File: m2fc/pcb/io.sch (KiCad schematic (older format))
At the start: 35 parts, among them IC401 ADuM5201, IC402 ADuM1201, P401 CONN_4, P402 CONN_2, P403 CONN_4, U401 HOUSING, U402 RG LED, U403 HOUSING, U404 HOUSING

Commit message: m2fc footprints, start layout
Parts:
- removed C401, C402: 10µ, m2fc:C0603, symbol CP1
- added C401, C402: 10µ, m2fc:C0603, symbol C
- IC401: footprint (none) -> m2fc:SOIC16
- IC402: Farnell (none) -> 1078200
- P401, P403: Farnell (none) -> 1830749
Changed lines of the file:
@@
 F 2 "m2fc:S04B-PASK-2" H 6150 3350 60  0001 C CNN
 F 3 "" H 6150 3350 60  0001 C CNN
-F 4 "512-8484" V 6150 3350 60  0001 C CNN "RS"
+F 4 "1830749" H 6150 3350 60  0001 C CNN "Farnell"
+F 5 "512-8484" V 6150 3350 60  0001 C CNN "RS"
 	1    6150 3350
 	1    0    0    -1
@@
 F 0 "IC401" H 4500 3800 60  0000 C CNN
 F 1 "ADuM5201" H 4650 2900 60  0000 C CNN
-F 2 "" H 4800 3400 60  0001 C CNN
+F 2 "m2fc:SOIC16" H 4800 3400 60  0001 C CNN
 F 3 "" H 4800 3400 60  0000 C CNN
 F 4 "2067773" H 4700 3400 60  0001 C CNN "Farnell"
@@
 $EndComp
 $Comp
-L CP1 C401
-U 1 1 53B6A643
-P 4000 2600
-F 0 "C401" H 4050 2700 50  0000 L CNN
-F 1 "10µ" H 4050 2500 50  0000 L CNN
-F 2 "m2fc:C0603" H 4000 2600 60  0001 C CNN
-F 3 "" H 4000 2600 60  0001 C CNN
-F 4 "1657936" H 4000 2600 60  0001 C CNN "Farnell"
-	1    4000 2600
-	0    1    -1   0
-$EndComp
-$Comp
 L C C404
 U 1 1 53B6A64B
@@
 $EndComp
 $Comp
-L CP1 C402
-U 1 1 53B6A653
-P 5450 2700
-F 0 "C402" H 5500 2800 50  0000 L CNN
-F 1 "10µ" H 5500 2600 50  0000 L CNN
-F 2 "m2fc:C0603" H 5450 2700 60  0001 C CNN
-F 3 "" H 5450 2700 60  0001 C CNN
-F 4 "1657936" H 5450 2700 60  0001 C CNN "Farnell"
-	1    5450 2700
-	0    -1   -1   0
-$EndComp
-$Comp
-L GND #PWR408
+L GND #PWR0129
 U 1 1 53B6A65A
 P 4200 3500
-F 0 "#PWR408" H 4200 3500 30  0001 C CNN
+F 0 "#PWR0129" H 4200 3500 30  0001 C CNN
 F 1 "GND" H 4200 3430 30  0001 C CNN
 F 2 "" H 4200 3500 60  0001 C CNN
@@
 $EndComp
 $Comp
-L GND #PWR411
+L GND #PWR0130
 U 1 1 53B6A660
 P 4250 3850
-F 0 "#PWR411" H 4250 3850 30  0001 C CNN
+F 0 "#PWR0130" H 4250 3850 30  0001 C CNN
 F 1 "GND" H 4250 3780 30  0001 C CNN
 F 2 "" H 4250 3850 60  0001 C CNN
@@
 $EndComp
 $Comp
-L GND #PWR406
+L GND #PWR0131
 U 1 1 53B6A668
 P 3750 3100
-F 0 "#PWR406" H 3750 3100 30  0001 C CNN
+F 0 "#PWR0131" H 3750 3100 30  0001 C CNN
 F 1 "GND" H 3750 3030 30  0001 C CNN
 F 2 "" H 3750 3100 60  0001 C CNN
@@
 SERIAL IN/OUT 1
 $Comp
-L +3.3V #PWR410
+L +3.3V #PWR0132
 U 1 1 53B6A6B9
 P 4100 3600
-F 0 "#PWR410" H 4100 3560 30  0001 C CNN
+F 0 "#PWR0132" H 4100 3560 30  0001 C CNN
 F 1 "+3.3V" H 4100 3710 30  0000 C CNN
 F 2 "" H 4100 3600 60  0000 C CNN
@@
 $EndComp
 $Comp
-L GND #PWR403
+L GND #PWR0133
 U 1 1 53B6B193
 P 7600 2550
-F 0 "#PWR403" H 7600 2550 30  0001 C CNN
+F 0 "#PWR0133" H 7600 2550 30  0001 C CNN
 F 1 "GND" H 7600 2480 30  0001 C CNN
 F 2 "" H 7600 2550 60  0001 C CNN
@@
 $EndComp
 $Comp
-L GND #PWR404
+L GND #PWR0134
 U 1 1 53B6B1AA
 P 7950 2800
-F 0 "#PWR404" H 7950 2800 30  0001 C CNN
+F 0 "#PWR0134" H 7950 2800 30  0001 C CNN
 F 1 "GND" H 7950 2730 30  0001 C CNN
 F 2 "" H 7950 2800 60  0001 C CNN
@@
 $EndComp
 $Comp
-L GND #PWR405
+L GND #PWR0135
 U 1 1 53B6B1C1
 P 7950 3050
-F 0 "#PWR405" H 7950 3050 30  0001 C CNN
+F 0 "#PWR0135" H 7950 3050 30  0001 C CNN
 F 1 "GND" H 7950 2980 30  0001 C CNN
 F 2 "" H 7950 3050 60  0001 C CNN
@@
 $EndComp
 $Comp
-L GND #PWR407
+L GND #PWR0136
 U 1 1 53B6B1D8
 P 7950 3300
-F 0 "#PWR407" H 7950 3300 30  0001 C CNN
+F 0 "#PWR0136" H 7950 3300 30  0001 C CNN
 F 1 "GND" H 7950 3230 30  0001 C CNN
 F 2 "" H 7950 3300 60  0001 C CNN
@@
 INTERNAL STATUS LEDS
 $Comp
-L +3.3V #PWR401
+L +3.3V #PWR0137
 U 1 1 53B6B1DF
 P 6550 2450
-F 0 "#PWR401" H 6550 2410 30  0001 C CNN
+F 0 "#PWR0137" H 6550 2410 30  0001 C CNN
 F 1 "+3.3V" H 6550 2560 30  0000 C CNN
 F 2 "" H 6550 2450 60  0000 C CNN
@@
 $EndComp
 $Comp
-L GND #PWR417
+L GND #PWR0138
 U 1 1 53BB3222
 P 7150 4800
-F 0 "#PWR417" H 7150 4800 30  0001 C CNN
+F 0 "#PWR0138" H 7150 4800 30  0001 C CNN
 F 1 "GND" H 7150 4730 30  0001 C CNN
 F 2 "" H 7150 4800 60  0001 C CNN
@@
 $EndComp
 $Comp
-L GND #PWR412
+L GND #PWR0139
 U 1 1 53BB32F5
 P 7150 4100
-F 0 "#PWR412" H 7150 4100 30  0001 C CNN
+F 0 "#PWR0139" H 7150 4100 30  0001 C CNN
 F 1 "GND" H 7150 4030 30  0001 C CNN
 F 2 "" H 7150 4100 60  0001 C CNN
@@
 INPUT/OUTPUT
 $Comp
-L +3.3V #PWR402
+L +3.3V #PWR0140
 U 1 1 53C7FC56
 P 4250 2550
-F 0 "#PWR402" H 4250 2510 30  0001 C CNN
+F 0 "#PWR0140" H 4250 2510 30  0001 C CNN
 F 1 "+3.3V" H 4250 2660 30  0000 C CNN
 F 2 "" H 4250 2550 60  0000 C CNN
@@
 F 2 "m2fc:S04B-PASK-2" H 6150 4550 60  0001 C CNN
 F 3 "" H 6150 4550 60  0001 C CNN
-F 4 "512-8484" V 6150 4550 60  0001 C CNN "RS"
+F 4 "1830749" H 6150 4550 60  0001 C CNN "Farnell"
+F 5 "512-8484" V 6150 4550 60  0001 C CNN "RS"
 	1    6150 4550
 	1    0    0    -1
@@
 $EndComp
 $Comp
-L +3.3V #PWR414
+L +3.3V #PWR0141
 U 1 1 53C90EC1
 P 4300 4350
-F 0 "#PWR414" H 4300 4310 30  0001 C CNN
+F 0 "#PWR0141" H 4300 4310 30  0001 C CNN
 F 1 "+3.3V" H 4300 4460 30  0000 C CNN
 F 2 "" H 4300 4350 60  0000 C CNN
@@
 F 2 "m2fc:SOIC8" H 4700 4550 60  0001 C CNN
 F 3 "" H 4700 4550 60  0000 C CNN
+F 4 "1078200" H 4700 4550 60  0001 C CNN "Farnell"
 	1    4700 4550
 	1    0    0    -1
 $EndComp
 $Comp
-L GND #PWR415
+L GND #PWR0142
 U 1 1 53C90E72
 P 4300 4750
-F 0 "#PWR415" H 4300 4750 30  0001 C CNN
+F 0 "#PWR0142" H 4300 4750 30  0001 C CNN
 F 1 "GND" H 4300 4680 30  0001 C CNN
 F 2 "" H 4300 4750 60  0001 C CNN
@@
 	6350 5300 8150 5300
 $Comp
-L PWR_FLAG #FLG401
+L PWR_FLAG #FLG0143
 U 1 1 53D4CBCD
 P 5750 4350
-F 0 "#FLG401" H 5750 4445 30  0001 C CNN
+F 0 "#FLG0143" H 5750 4445 30  0001 C CNN
 F 1 "PWR_FLAG" H 5750 4530 30  0000 C CNN
 F 2 "" H 5750 4350 60  0000 C CNN
@@
 $EndComp
 $Comp
-L PWR_FLAG #FLG402
+L PWR_FLAG #FLG0144
 U 1 1 53D4CC1D
 P 5750 4750
-F 0 "#FLG402" H 5750 4845 30  0001 C CNN
+F 0 "#FLG0144" H 5750 4845 30  0001 C CNN
 F 1 "PWR_FLAG" H 5750 4930 30  0000 C CNN
 F 2 "" H 5750 4750 60  0000 C CNN
@@
 $EndComp
 $Comp
-L GND #PWR409
+L GND #PWR0145
 U 1 1 53D79DC5
 P 7950 3550
-F 0 "#PWR409" H 7950 3550 30  0001 C CNN
+F 0 "#PWR0145" H 7950 3550 30  0001 C CNN
 F 1 "GND" H 7950 3480 30  0001 C CNN
 F 2 "" H 7950 3550 60  0001 C CNN
@@
 Connection ~ 7600 4150
 $Comp
-L GND #PWR413
+L GND #PWR0146
 U 1 1 53DA7B01
 P 7900 4200
-F 0 "#PWR413" H 7900 4200 30  0001 C CNN
+F 0 "#PWR0146" H 7900 4200 30  0001 C CNN
 F 1 "GND" H 7900 4130 30  0001 C CNN
 F 2 "" H 7900 4200 60  0001 C CNN
@@
 	7900 4150 7900 4200
 $Comp
-L GND #PWR416
+L GND #PWR0147
 U 1 1 53DA7BD9
 P 7900 4750
-F 0 "#PWR416" H 7900 4750 30  0001 C CNN
+F 0 "#PWR0147" H 7900 4750 30  0001 C CNN
 F 1 "GND" H 7900 4680 30  0001 C CNN
 F 2 "" H 7900 4750 60  0001 C CNN
@@
 Wire Wire Line
 	7900 4700 7900 4750
+$Comp
+L C C402
+U 1 1 53D87AE9
+P 5450 2700
+F 0 "C402" H 5500 2800 50  0000 L CNN
+F 1 "10µ" H 5500 2600 50  0000 L CNN
+F 2 "m2fc:C0603" H 5450 2700 60  0001 C CNN
+F 3 "" H 5450 2700 60  0001 C CNN
+F 4 "2211164" H 5450 2700 60  0001 C CNN "Farnell"
+	1    5450 2700
+	0    -1   -1   0
+$EndComp
+$Comp
+L C C401
+U 1 1 53D87C19
+P 4000 2600
+F 0 "C401" H 4050 2700 50  0000 L CNN
+F 1 "10µ" H 4050 2500 50  0000 L CNN
+F 2 "m2fc:C0603" H 4000 2600 60  0001 C CNN
+F 3 "" H 4000 2600 60  0001 C CNN
+F 4 "2211164" H 4000 2600 60  0001 C CNN "Farnell"
+	1    4000 2600
+	0    -1   -1   0
+$EndComp
 $EndSCHEMATC

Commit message: layout going ok so far...
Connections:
- net GND: now also D407.1; no longer D407.2
- net LED_C: now also D407.2; no longer D407.1
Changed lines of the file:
@@
 L CGA0402MLC-12G D407
 U 1 1 53DA782A
-P 7650 4700
-F 0 "D407" H 7750 4600 60  0000 C CNN
-F 1 "CGA0402MLC-12G" H 7750 4810 60  0001 C CNN
-F 2 "m2fc:R0402" H 7650 4700 60  0001 C CNN
-F 3 "" H 7650 4700 60  0000 C CNN
-F 4 "2368169" H 7650 4700 60  0001 C CNN "Farnell"
-	1    7650 4700
-	1    0    0    -1
+P 7850 4700
+F 0 "D407" H 7950 4600 60  0000 C CNN
+F 1 "CGA0402MLC-12G" H 7950 4810 60  0001 C CNN
+F 2 "m2fc:R0402" H 7850 4700 60  0001 C CNN
+F 3 "" H 7850 4700 60  0000 C CNN
+F 4 "2368169" H 7850 4700 60  0001 C CNN "Farnell"
+	1    7850 4700
+	-1   0    0    1
 $EndComp
 Wire Wire Line

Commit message: flip around power connectors
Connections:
- net SER_IN_2: now also IC402.2 (OUT_A), TP403.1 (TP); no longer IC402.3 (IN_B), TP404.1 (TP)
- net SER_OUT_2: now also IC402.3 (IN_B), TP404.1 (TP); no longer IC402.2 (OUT_A), TP403.1 (TP)
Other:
- note added: "NB Different Serial Pinouts"
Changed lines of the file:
@@
 Text Notes 3350 5250 0    60   ~ 0
 SERIAL IN/OUT 2
-Text HLabel 4000 4500 0    60   Input ~ 0
+Text HLabel 4000 4600 0    60   Input ~ 0
 SER_OUT_2
-Text HLabel 4000 4600 0    60   Output ~ 0
+Text HLabel 4000 4500 0    60   Output ~ 0
 SER_IN_2
 $Comp
@@
 	0    -1   -1   0
 $EndComp
+Text Notes 3350 5100 0    60   ~ 0
+NB Different Serial Pinouts
 $EndSCHEMATC

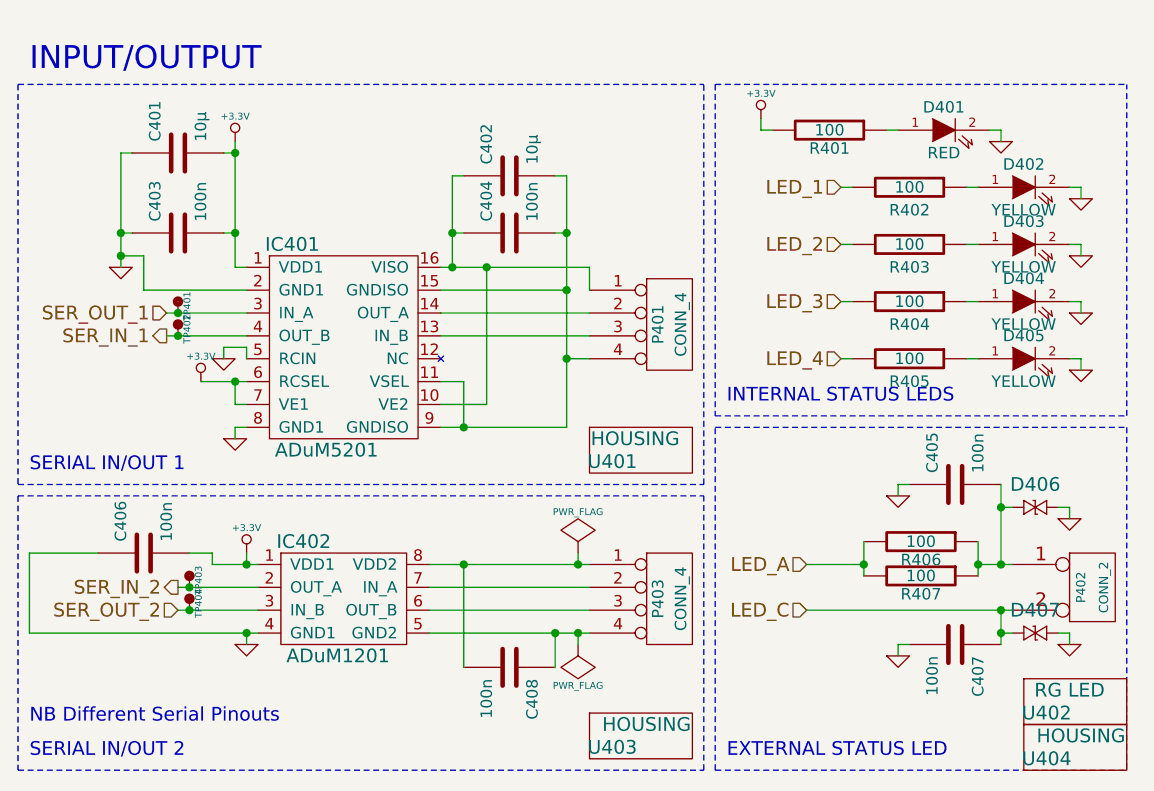
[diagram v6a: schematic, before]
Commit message: 3V ANALOG LED
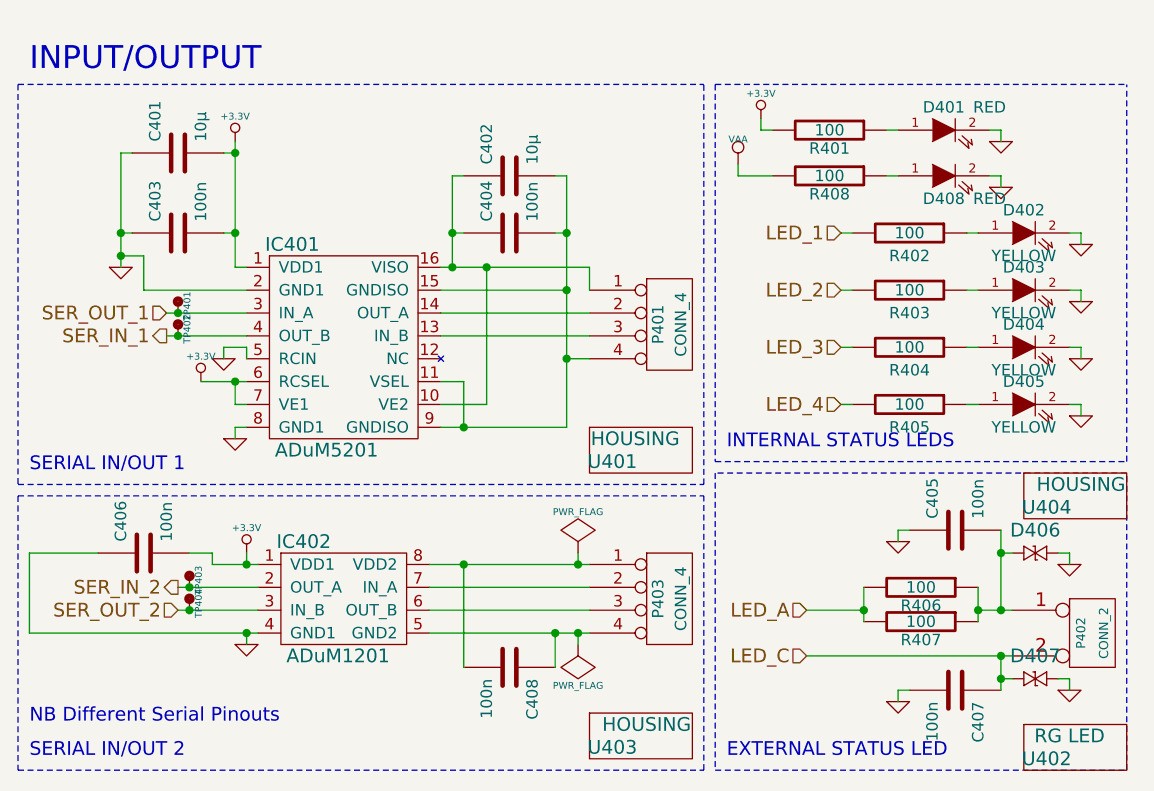
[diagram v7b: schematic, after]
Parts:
- added D408: RED, m2fc:LED0603, symbol LED
- added R408: 100, m2fc:R0603, symbol R
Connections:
- net GND: now also D408.2 (K)
- new net: D408.1 (A), R408.1
- new net VAA: R408.2
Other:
- moved on the sheet: C405, C407, D402, D403, D404, D405, D406, D407, P402, R402, R403, R404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

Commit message: rescue symbols from m2fc pcb
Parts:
- C401, C402, C403, C404, C405, C406, C407, C408: symbol C -> C-RESCUE-m2fc
- D401, D402, D403, D404, D405, D408: symbol LED -> LED-RESCUE-m2fc
- R401, R402, R403, R404, R405, R406, R407, R408: symbol R -> R-RESCUE-m2fc
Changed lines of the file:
@@
 EESchema Schematic File Version 2
+LIBS:m2fc-rescue
 LIBS:power
 LIBS:device
@@
 LIBS:memory
 LIBS:xilinx
-LIBS:special
 LIBS:microcontrollers
 LIBS:dsp
@@
 LIBS:cga0402mlc-12g
 LIBS:m2fc-cache
-EELAYER 24 0
+EELAYER 25 0
 EELAYER END
 $Descr A4 11693 8268
@@
 $EndComp
 $Comp
-L C C403
+L C-RESCUE-m2fc C403
 U 1 1 53B6A63B
 P 4000 2950
@@
 $EndComp
 $Comp
-L C C404
+L C-RESCUE-m2fc C404
 U 1 1 53B6A64B
 P 5450 2950
@@
 $EndComp
 $Comp
-L GND #PWR0134
+L GND-RESCUE-m2fc #PWR0134
 U 1 1 53B6A65A
 P 4200 3500
@@
 $EndComp
 $Comp
-L GND #PWR0135
+L GND-RESCUE-m2fc #PWR0135
 U 1 1 53B6A660
 P 4250 3850
@@
 $EndComp
 $Comp
-L GND #PWR0136
+L GND-RESCUE-m2fc #PWR0136
 U 1 1 53B6A668
 P 3750 3100
@@
 SERIAL IN/OUT 1
 $Comp
-L +3.3V #PWR0137
+L +3.3V-RESCUE-m2fc #PWR0137
 U 1 1 53B6A6B9
 P 4100 3600
@@
 $EndComp
 $Comp
-L R R407
+L R-RESCUE-m2fc R407
 U 1 1 53B6AD98
 P 7250 4650
@@
 $EndComp
 $Comp
-L R R406
+L R-RESCUE-m2fc R406
 U 1 1 53B6ADA0
 P 7250 4500
@@
 $EndComp
 $Comp
-L LED D401
+L LED-RESCUE-m2fc D401
 U 1 1 53B6B184
 P 7350 2500
@@
 $EndComp
 $Comp
-L R R401
+L R-RESCUE-m2fc R401
 U 1 1 53B6B18C
 P 6850 2500
@@
 $EndComp
 $Comp
-L GND #PWR0138
+L GND-RESCUE-m2fc #PWR0138
 U 1 1 53B6B193
 P 7600 2550
@@
 $EndComp
 $Comp
-L LED D402
+L LED-RESCUE-m2fc D402
 U 1 1 53B6B19B
 P 7700 2950
@@
 $EndComp
 $Comp
-L R R402
+L R-RESCUE-m2fc R402
 U 1 1 53B6B1A3
 P 7200 2950
@@
 $EndComp
 $Comp
-L GND #PWR0139
+L GND-RESCUE-m2fc #PWR0139
 U 1 1 53B6B1AA
 P 7950 3000
@@
 $EndComp
 $Comp
-L LED D403
+L LED-RESCUE-m2fc D403
 U 1 1 53B6B1B2
 P 7700 3200
@@
 $EndComp
 $Comp
-L R R403
+L R-RESCUE-m2fc R403
 U 1 1 53B6B1BA
 P 7200 3200
@@
 $EndComp
 $Comp
-L GND #PWR0140
+L GND-RESCUE-m2fc #PWR0140
 U 1 1 53B6B1C1
 P 7950 3250
@@
 $EndComp
 $Comp
-L LED D404
+L LED-RESCUE-m2fc D404
 U 1 1 53B6B1C9
 P 7700 3450
@@
 $EndComp
 $Comp
-L R R404
+L R-RESCUE-m2fc R404
 U 1 1 53B6B1D1
 P 7200 3450
@@
 $EndComp
 $Comp
-L GND #PWR0141
+L GND-RESCUE-m2fc #PWR0141
 U 1 1 53B6B1D8
 P 7950 3500
@@
 INTERNAL STATUS LEDS
 $Comp
-L +3.3V #PWR0142
+L +3.3V-RESCUE-m2fc #PWR0142
 U 1 1 53B6B1DF
 P 6550 2450
@@
 $EndComp
 $Comp
-L C C407
+L C-RESCUE-m2fc C407
 U 1 1 53BB2BD1
 P 7400 4950
@@
 $EndComp
 $Comp
-L C C405
+L C-RESCUE-m2fc C405
 U 1 1 53BB30F0
 P 7400 4250
@@
 $EndComp
 $Comp
-L GND #PWR0143
+L GND-RESCUE-m2fc #PWR0143
 U 1 1 53BB3222
 P 7150 5000
@@
 $EndComp
 $Comp
-L GND #PWR0144
+L GND-RESCUE-m2fc #PWR0144
 U 1 1 53BB32F5
 P 7150 4300
@@
 INPUT/OUTPUT
 $Comp
-L +3.3V #PWR0145
+L +3.3V-RESCUE-m2fc #PWR0145
 U 1 1 53C7FC56
 P 4250 2550
@@
 $EndComp
 $Comp
-L C C406
+L C-RESCUE-m2fc C406
 U 1 1 53C90E4B
 P 3850 4350
@@
 $EndComp
 $Comp
-L C C408
+L C-RESCUE-m2fc C408
 U 1 1 53C90E59
 P 5450 4850
@@
 $EndComp
 $Comp
-L +3.3V #PWR0146
+L +3.3V-RESCUE-m2fc #PWR0146
 U 1 1 53C90EC1
 P 4300 4350
@@
 $EndComp
 $Comp
-L GND #PWR0147
+L GND-RESCUE-m2fc #PWR0147
 U 1 1 53C90E72
 P 4300 4750
@@
 Connection ~ 5750 4400
 $Comp
-L LED D405
+L LED-RESCUE-m2fc D405
 U 1 1 53D79DB8
 P 7700 3700
@@
 $EndComp
 $Comp
-L R R405
+L R-RESCUE-m2fc R405
 U 1 1 53D79DBF
 P 7200 3700
@@
 $EndComp
 $Comp
-L GND #PWR0150
+L GND-RESCUE-m2fc #PWR0150
 U 1 1 53D79DC5
 P 7950 3750
@@
 Connection ~ 7600 4350
 $Comp
-L GND #PWR0151
+L GND-RESCUE-m2fc #PWR0151
 U 1 1 53DA7B01
 P 7900 4400
@@
 	7900 4350 7900 4400
 $Comp
-L GND #PWR0152
+L GND-RESCUE-m2fc #PWR0152
 U 1 1 53DA7BD9
 P 7900 4950
@@
 	7900 4900 7900 4950
 $Comp
-L C C402
+L C-RESCUE-m2fc C402
 U 1 1 53D87AE9
 P 5450 2700
@@
 $EndComp
 $Comp
-L C C401
+L C-RESCUE-m2fc C401
 U 1 1 53D87C19
 P 4000 2600
@@
 	8150 3950 8150 2300
 $Comp
-L LED D408
+L LED-RESCUE-m2fc D408
 U 1 1 53DC6F1D
 P 7350 2700
@@
 $EndComp
 $Comp
-L R R408
+L R-RESCUE-m2fc R408
 U 1 1 53DC6F24
 P 6850 2700
@@
 $EndComp
 $Comp
-L GND #PWR0153
+L GND-RESCUE-m2fc #PWR0153
 U 1 1 53DC6F2A
 P 7600 2750
